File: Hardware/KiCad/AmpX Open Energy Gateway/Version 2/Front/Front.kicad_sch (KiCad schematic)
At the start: 11 parts, among them J3 Status Conn Top

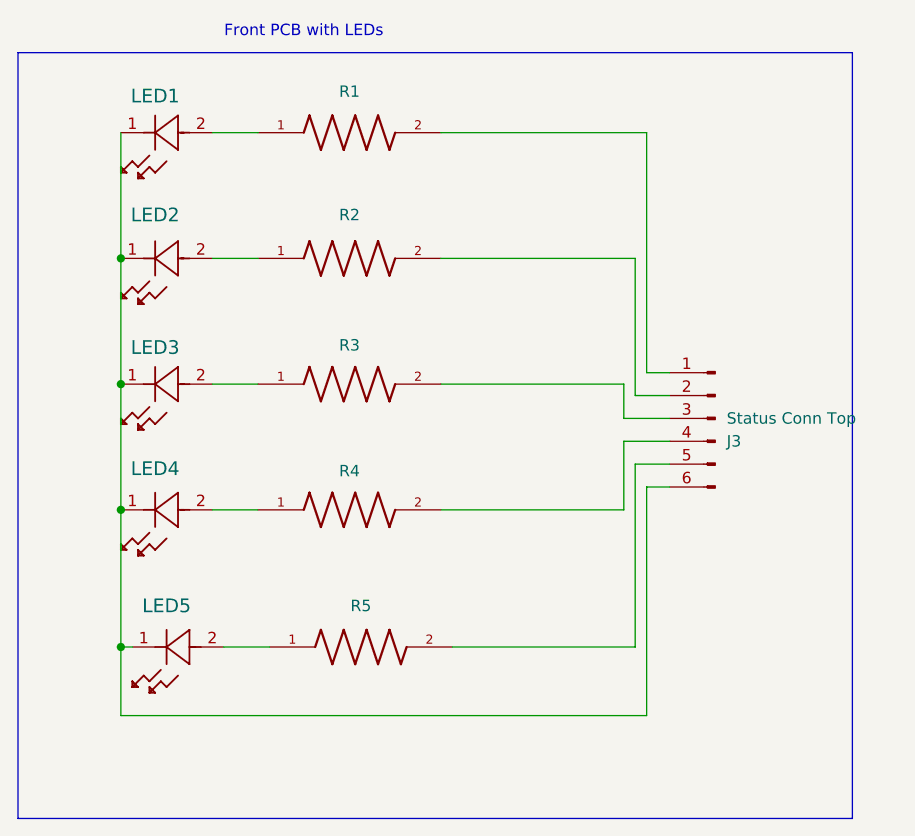
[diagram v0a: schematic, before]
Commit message: added extra wire for ground
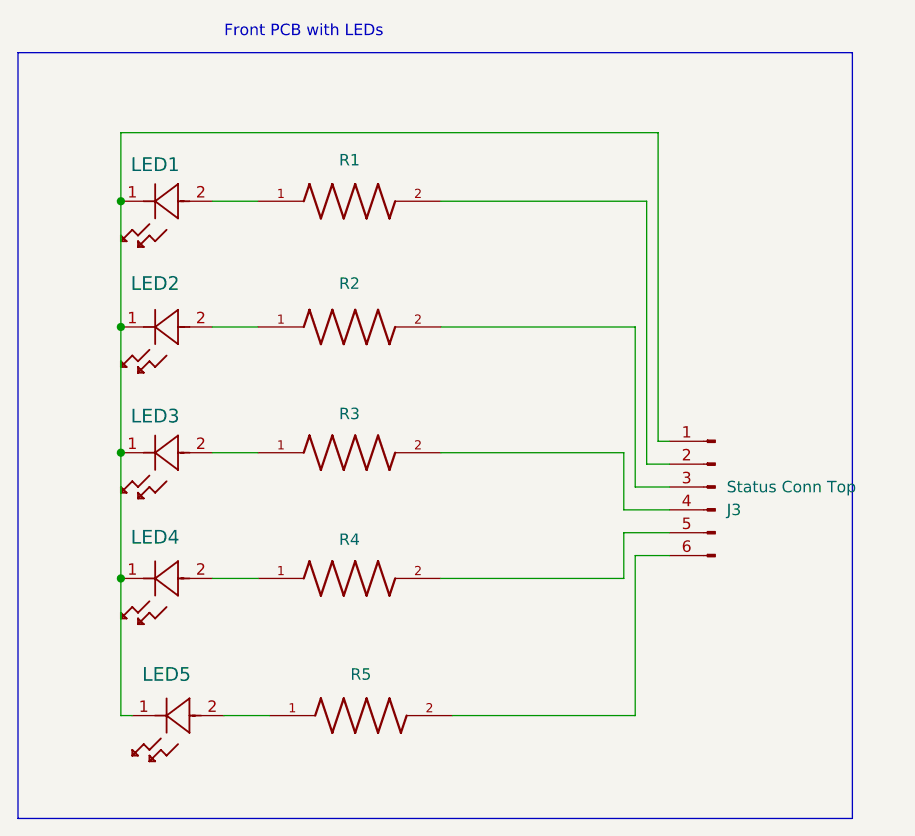
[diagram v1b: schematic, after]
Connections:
- net at LED1.1, LED2.1, LED3.1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: now also J3.1 (Pin_1); no longer J3.6 (Pin_6)
- net at R5.2: now also J3.6 (Pin_6); no longer J3.5 (Pin_5)
- net at R3.2: now also J3.4 (Pin_4); no longer J3.3 (Pin_3)
- net at R2.2: now also J3.3 (Pin_3); no longer J3.2 (Pin_2)
- net at R1.2: now also J3.2 (Pin_2); no longer J3.1 (Pin_1)
- net at R4.2: now also J3.5 (Pin_5); no longer J3.4 (Pin_4)
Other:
- moved on the sheet: J3, LED1, LED2, LED3, LED4, LED5, R1, R2, R3, R4, R5
